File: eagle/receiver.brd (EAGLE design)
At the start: 82.5 x 47.6 mm, 231 parts, among them U1 LTC5566, U4 LTC5566

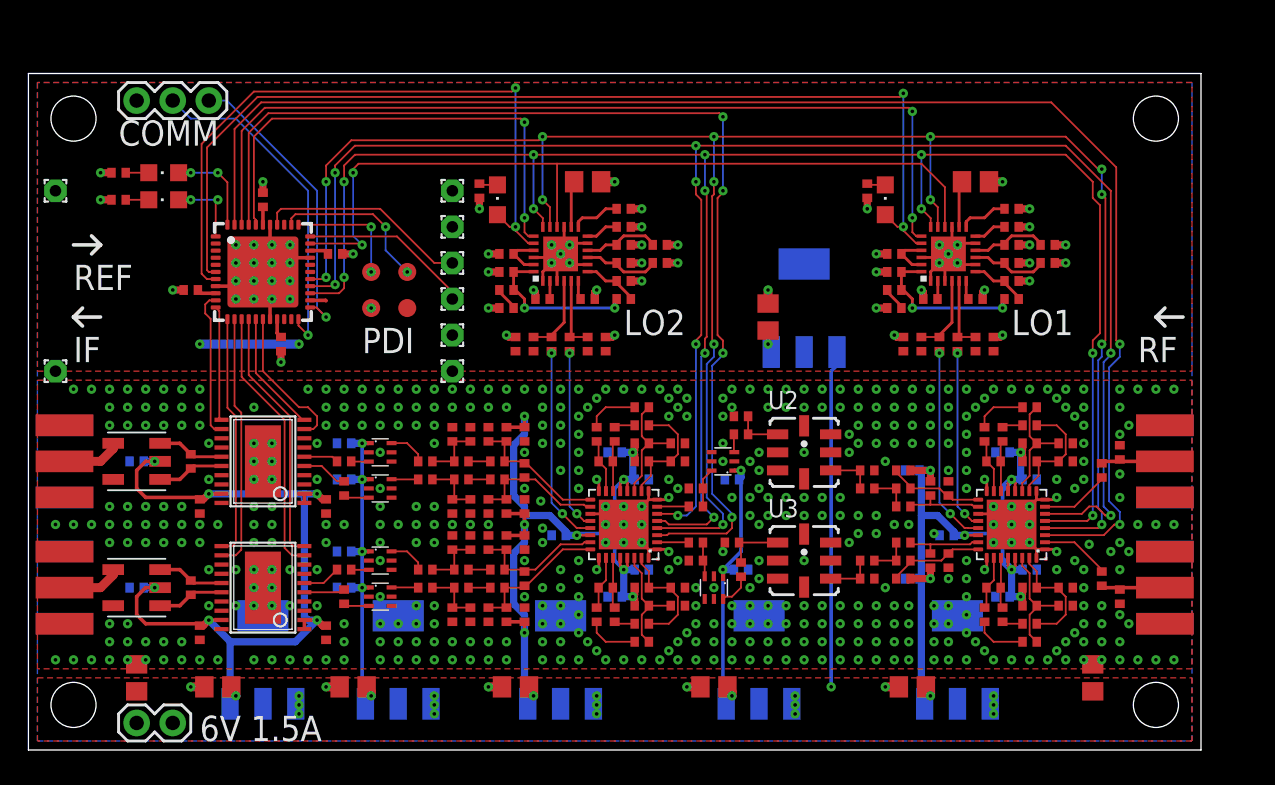
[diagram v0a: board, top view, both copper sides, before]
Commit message: fix issue with receiver board
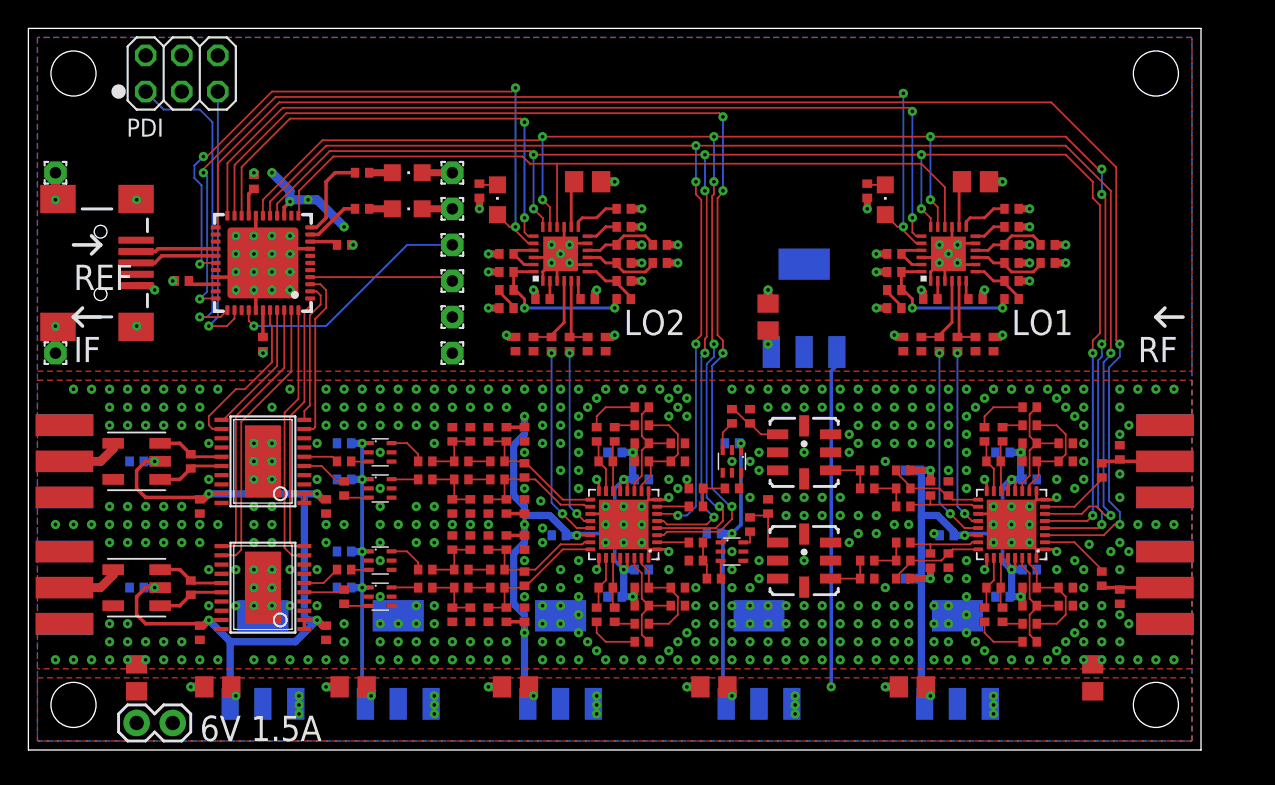
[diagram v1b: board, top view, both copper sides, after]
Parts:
- removed E$21: (no value), atmel:MLF44-TH
- removed E$38: (no value), SparkFun-Connectors:1X03
- removed E$39, E$40, E$41, E$42: (no value), testpad:B1,27
- removed E$45, E$46: (no value), led:CHIPLED_0805
- removed L8: (no value), rcl:R0402
- added D1, D2: (no value), led:CHIPLED_0805
- added J1: (no value), SparkFun-Connectors:USB-MINIB
- added PDI: (no value), pinhead:2X03
- added R1, R2: 330, rcl:R0402
- added R6: 100, rcl:R0402
- added U9: (no value), atmel:MLF44-TH
- C103, C104, C117, C118, C123, C124, C125, C126, C129, C130, C131, C163, C164, C71, C72, C73, C74, C75, C76, C89, C90: value (none) -> 100n
- C132: value (none) -> 1--n
- C45, C77, C78, C81, C82, C83, C84, C87, C88: value (none) -> 10n
- C46: value (none) -> 18p
- C79, C80, C85, C86: value (none) -> 22n
- L3: value (none) -> 11n
- R5: value (none) -> 100
- moved C45 47.7 mm to (49.5, 18.4), turned to 180 degrees
- moved C44 46.5 mm to (49.5, 23.5), turned to 270 degrees
- moved C127 16.3 mm to (50.8, 15.9)
- moved L5 3.59 mm to (52.1, 17.1), turned to 90 degrees
- moved L10 3.18 mm to (48.3, 15.2), turned to 180 degrees
- moved E$5 2.84 mm to (49.5, 14.0), turned to 270 degrees
- moved L9 2.54 mm to (49.5, 21.6)
- moved L6 2.01 mm to (48.3, 12.1), turned to 180 degrees
- moved C71 1.42 mm to (15.9, 40.0)
- moved E$29 1.27 mm to (1.91, 40.6)
- moved E$30 1.27 mm to (29.8, 40.6)
- moved E$33 1.27 mm to (29.8, 35.6)
- moved E$34 1.27 mm to (29.8, 33.0)
- moved E$35 1.27 mm to (29.8, 38.1)
- moved C76 1.27 mm to (16.5, 28.6)
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- renumbered C128 to R5, C161 to R3, C162 to R4, E$1 to J5, E$15 to U5, E$16 to U6, E$17 to J2, E$18 to J3, E$2 to J6, E$3 to U7, E$4 to U8, E$51 to J4, E$52 to T1, E$53 to T2
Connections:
- removed net S$49: E$6.3, L8.2
- removed net S$87: E$13.11, E$21.11
- removed net S$88: E$13.12, E$21.10
- new net LOCK0: E$47.A, U8.20, U9.28
- new net LOCK1: E$48.A, U7.20, U9.33
- new net S$1: J1.D-, U9.26
- new net S$115: E$13.11, U9.41
- new net S$2: J1.D+, U9.27
- net !RESET: now also PDI.5, U9.35; no longer E$21.35, E$40.TP
- net CLK: now also U9.37; no longer E$21.37
- net CLK_100K: now also U9.12; no longer E$21.32
- net CS0: now also U9.20; no longer E$21.40
- net CS1: now also U9.21; no longer E$21.41
- net CS2: now also U9.22; no longer E$21.42
- net CS3: now also U9.23; no longer E$21.43
- net GND: now also D1.C, D2.C, J1.GND, J1.S1, J1.S2, J1.S3, J1.S4, PDI.6, U9.18, U9.30, U9.38, U9.8, U9.TH; no longer C44.1, C45.1, E$21.18, E$21.30, E$21.38, E$21.8, E$21.TH, E$38.1, E$42.TP
- net PDI: now also PDI.1, U9.34; no longer E$21.34, E$41.TP
- net PPS: now also U9.4; no longer E$21.33
- net S$106: now also D1.A, R1.1; no longer C45.2, E$46.C
- net S$109: now also D2.A, R2.1; no longer E$21.44, E$45.A
- net S$110: now also E$13.12, U9.40; no longer E$21.1, E$46.A
- net S$27: now also R1.2, U9.11; no longer E$21.7, E$47.A, U8.20
- net S$28: now also R2.2, U9.10; no longer E$21.23, E$38.3
- net S$29: now also L6.2; no longer E$5.3
- net S$30: now also C45.2; no longer E$6.6
- net S$47: now also R6.1; no longer C127.1
- net S$48: now also R6.2; no longer C127.2
- net S$50: now also C127.1; no longer L6.2
- net S$52: now also C44.1; no longer L8.1
- net S$53: now also C127.2; no longer L6.1
- net S$56: now also C44.2, E$6.3; no longer E$21.22, E$38.2
- net S$69: now also U9.2; no longer E$21.16
- net S$82: now also U9.3; no longer E$21.17
- net S$83: now also U9.1; no longer E$21.15
- net S$84: now also U9.44; no longer E$21.14
- net S$85: now also U9.43; no longer E$21.13
- net S$86: now also U9.42; no longer E$21.12
- net S$96: now also E$5.3, L6.1; no longer E$21.6, E$48.A, U7.20
- net S$97: now also C45.1, E$6.6; no longer C44.2, E$45.C
- net SPI_CLK: now also U9.17; no longer E$21.27
- net SPI_SDI: now also U9.15; no longer E$21.25
- net SPI_SDO: now also U9.16; no longer E$21.26
- net V3.3: now also PDI.2, U9.14, U9.19, U9.31, U9.39, U9.9; no longer E$21.19, E$21.24, E$21.31, E$21.39, E$21.9, E$39.TP
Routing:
- net LOCK1: track 0.00 -> 75.0 mm, vias 0 -> 4
- net S$96: track 73.0 -> 1.27 mm, vias 2 -> 0
- net LOCK0: track 0.00 -> 46.5 mm, vias 0 -> 4
- net S$27: track 47.5 -> 6.24 mm, vias 2 -> 0
- net S$56: track 23.7 -> 2.14 mm, vias 1 -> 0
- net S$28: track 20.8 -> 3.91 mm, vias 1 -> 0
- net PDI: track 8.36 -> 22.1 mm, vias 2 -> 1
- net S$88: track 10.4 -> 0.00 mm
- net S$115: track 0.00 -> 9.42 mm
- net S$87: track 8.08 -> 0.00 mm
- net !RESET: track 11.4 -> 19.4 mm, vias 2 -> 1
- net S$110: track 5.40 -> 11.4 mm, vias 2 -> 0
- net GND: track 76.7 -> 82.6 mm, vias 549 -> 544
- net S$2: track 0.00 -> 5.81 mm
- net S$1: track 0.00 -> 5.69 mm
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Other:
- board size 82.5 x 47.6 mm -> 82.5 x 50.8 mm
- board text removed: "COMM"
- board text removed: "PDI"

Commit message: add power injection to receiver board
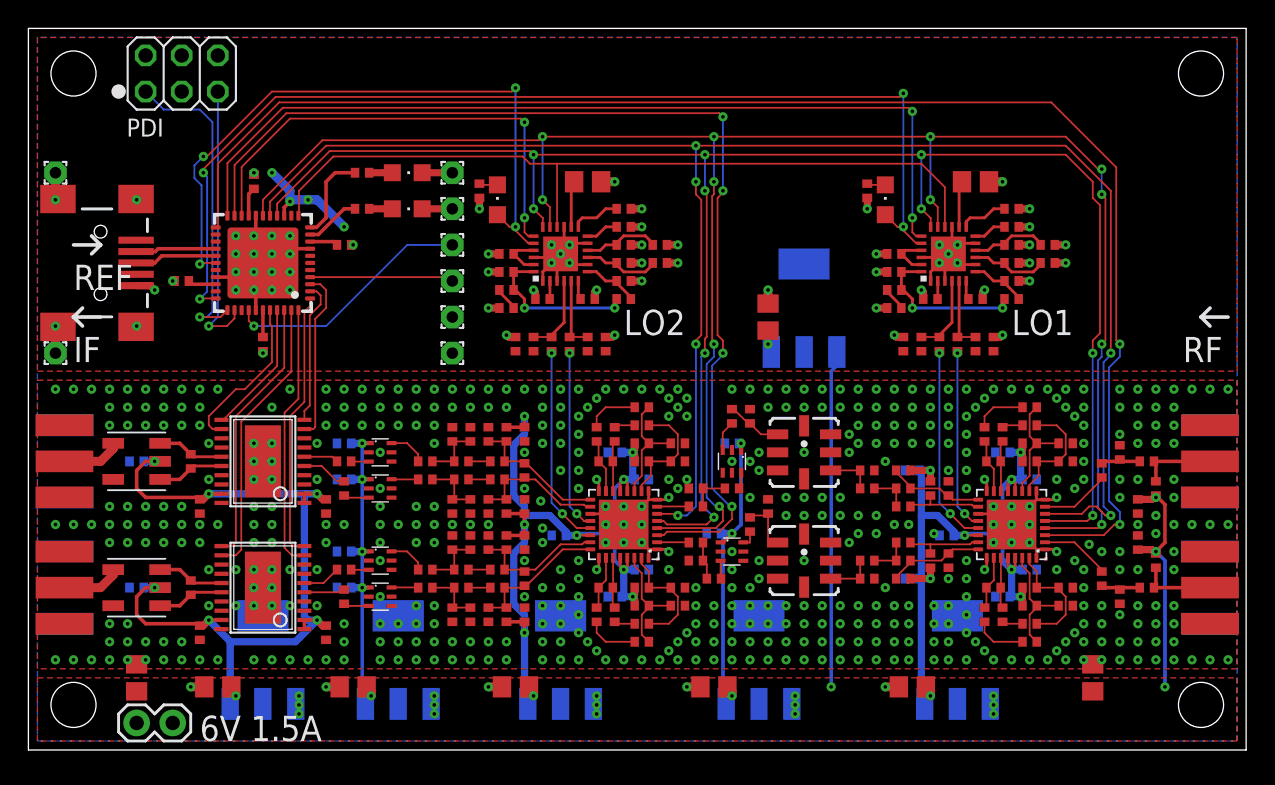
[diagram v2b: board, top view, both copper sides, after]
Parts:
- added C128, C161, C162, C165: 10n, rcl:R0402
- added L11, L8: 22n, rcl:R0402
- C1, C2: value (none) -> 2.8p
- C47: value (none) -> 18p
- E$23, E$24, E$25, E$27, E$49, E$50, E$8: value (none) -> 1u
- L1, L2: value (none) -> 5.8n
- L4: value (none) -> 11n
- L6: value (none) -> 10n
- moved J5 3.17 mm to (83.2, 8.89)
- moved J6 3.17 mm to (83.2, 17.8)
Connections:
- new net S$116: C1.1, C161.1, L1.1
- new net S$117: C128.1, C2.2, L2.1
- net GND: now also C162.1, C165.2
- net RF1: now also C161.2, L8.1; no longer C1.1, L1.1
- net RF2: now also C128.2, L11.2; no longer C2.2, L2.1
- net VIN: now also C162.2, C165.1, L11.1, L8.2
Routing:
- net VIN: track 25.0 -> 42.3 mm, vias 16 -> 19
- net S$117: track 0.00 -> 2.87 mm
- net S$116: track 0.00 -> 2.87 mm
- net RF2: track 4.64 -> 5.35 mm
- net RF1: track 4.64 -> 5.35 mm
- net GND: vias 544 -> 576
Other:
- board size 82.5 x 50.8 mm -> 85.7 x 50.8 mm

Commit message: tweak rf matching network
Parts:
- C1, C2: value 2.8p -> 3p
- L1, L2: value 5.8n -> 7.5n
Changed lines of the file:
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@@
 <element name="J5" library="SparkFun-Retired" library_urn="urn:adsk.eagle:library:533" package="SMA-EDGE" value="" x="83.185" y="8.89" smashed="yes" rot="R90"/>
 <element name="J6" library="SparkFun-Retired" library_urn="urn:adsk.eagle:library:533" package="SMA-EDGE" value="" x="83.185" y="17.78" smashed="yes" rot="R90"/>
-<element name="L1" library="rcl" library_urn="urn:adsk.eagle:library:334" package="R0402" package3d_urn="urn:adsk.eagle:package:23547/3" value="5.8n" x="76.835" y="20.955" smashed="yes" rot="R90"/>
-<element name="C1" library="rcl" library_urn="urn:adsk.eagle:library:334" package="R0402" package3d_urn="urn:adsk.eagle:package:23547/3" value="2.8p" x="75.565" y="19.685" smashed="yes" rot="R270"/>
-<element name="L2" library="rcl" library_urn="urn:adsk.eagle:library:334" package="R0402" package3d_urn="urn:adsk.eagle:package:23547/3" value="5.8n" x="76.835" y="10.795" smashed="yes" rot="R270"/>
-<element name="C2" library="rcl" library_urn="urn:adsk.eagle:library:334" package="R0402" package3d_urn="urn:adsk.eagle:package:23547/3" value="2.8p" x="75.565" y="12.065" smashed="yes" rot="R270"/>
+<element name="L1" library="rcl" library_urn="urn:adsk.eagle:library:334" package="R0402" package3d_urn="urn:adsk.eagle:package:23547/3" value="7.5n" x="76.835" y="20.955" smashed="yes" rot="R90"/>
+<element name="C1" library="rcl" library_urn="urn:adsk.eagle:library:334" package="R0402" package3d_urn="urn:adsk.eagle:package:23547/3" value="3p" x="75.565" y="19.685" smashed="yes" rot="R270"/>
+<element name="L2" library="rcl" library_urn="urn:adsk.eagle:library:334" package="R0402" package3d_urn="urn:adsk.eagle:package:23547/3" value="7.5n" x="76.835" y="10.795" smashed="yes" rot="R270"/>
+<element name="C2" library="rcl" library_urn="urn:adsk.eagle:library:334" package="R0402" package3d_urn="urn:adsk.eagle:package:23547/3" value="3p" x="75.565" y="12.065" smashed="yes" rot="R270"/>
 <element name="U1" library="ref-packages" library_urn="urn:adsk.eagle:library:338" package="HVQFN32" value="LTC5566" x="69.215" y="15.875" smashed="yes" rot="R180"/>
 <element name="C3" library="rcl" library_urn="urn:adsk.eagle:library:334" package="R0402" package3d_urn="urn:adsk.eagle:package:23547/3" value="" x="70.485" y="11.43" smashed="yes">

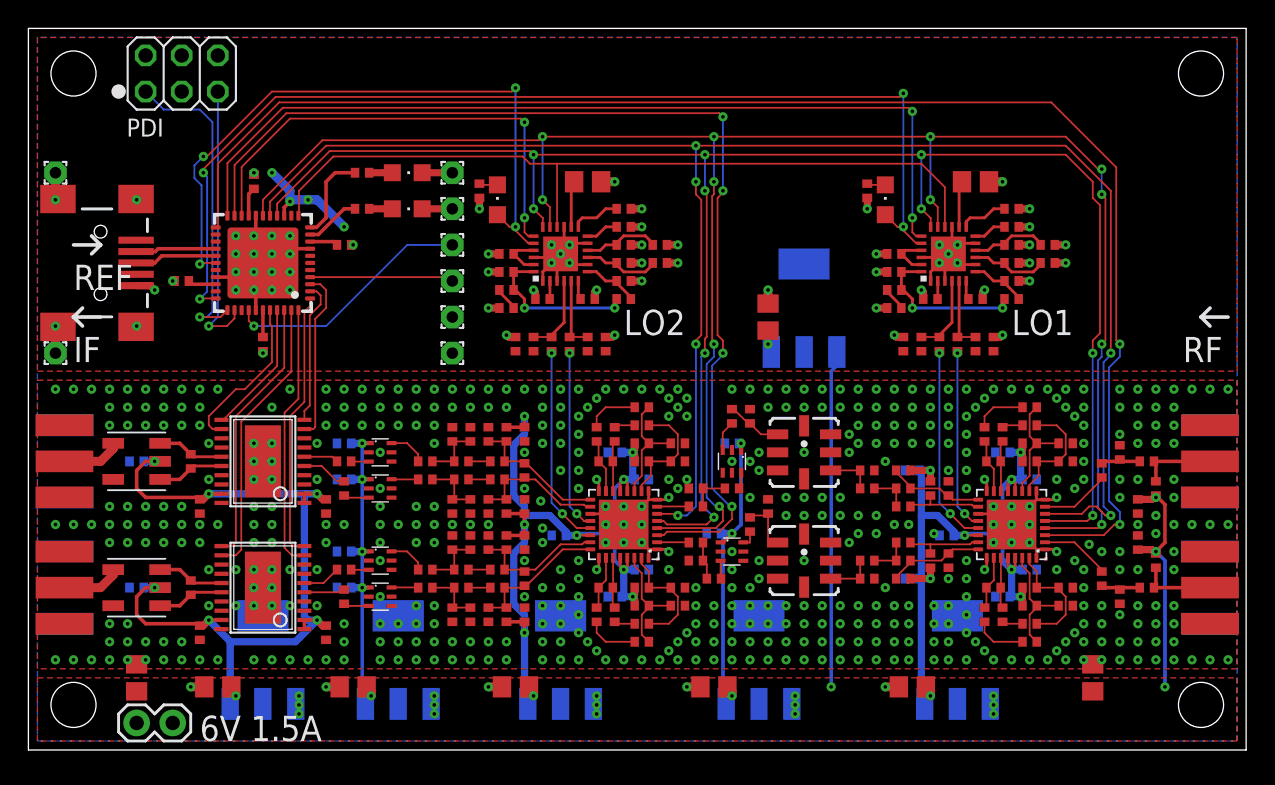
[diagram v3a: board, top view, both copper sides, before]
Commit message: fix saw filter matching
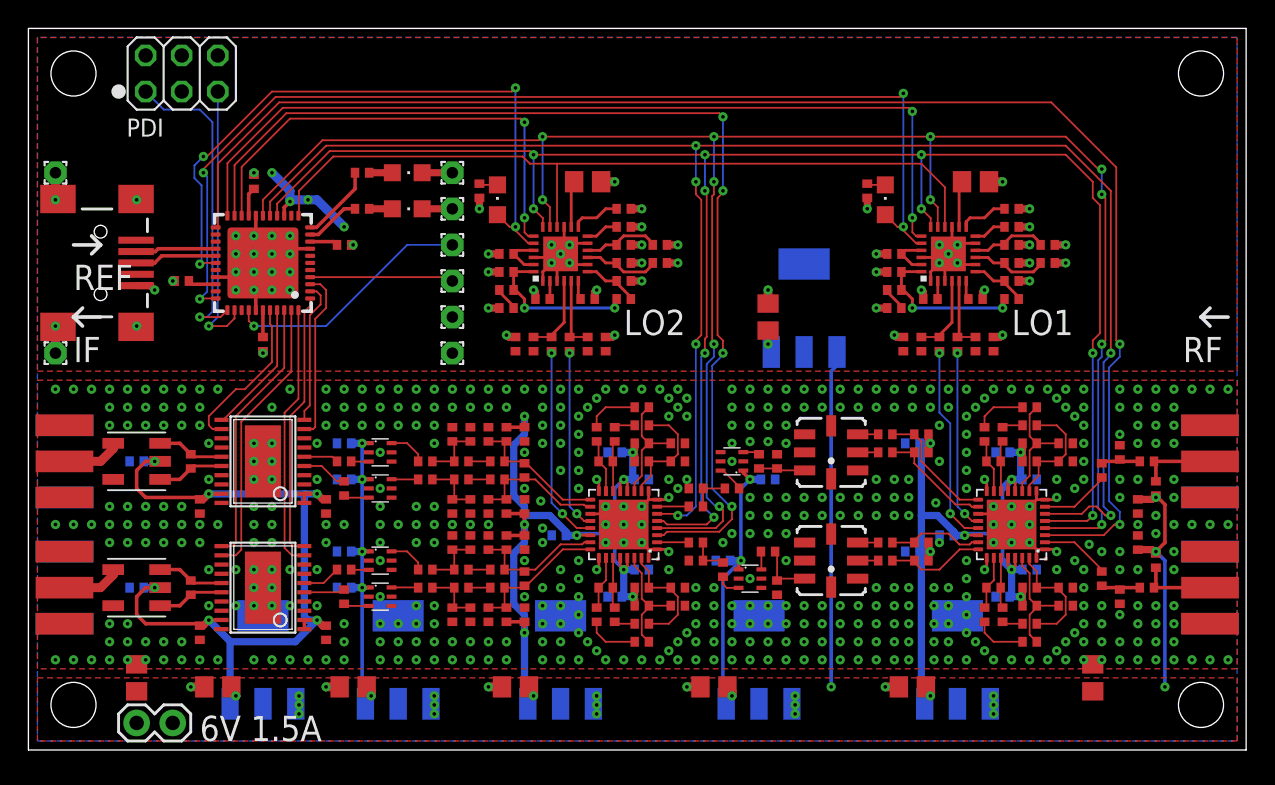
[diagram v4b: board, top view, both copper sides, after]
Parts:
- removed C28, C29, C31, C32, C34, C35, C36, C37, C39, C41: (no value), rcl:R0402
- added L12, L13, L14, L15: 13n, rcl:R0402
- C127, C44: value (none) -> 7p
- C30, C33, C38, C40: value (none) -> 470p
- C42, C43: value (none) -> 10n
- E$44: value (none) -> 1u
- L5, L7: value (none) -> 12n
- U2, U3: value (none) -> AFS374E
- moved L5 5.75 mm to (52.7, 11.4), turned to 270 degrees
- moved C33 4.02 mm to (60.3, 22.2)
- moved C44 3.70 mm to (51.4, 20.3), turned to 90 degrees
- moved L7 3.70 mm to (52.7, 20.3)
- moved L9 3.59 mm to (52.1, 19.1), turned to 0 degrees
- moved C30 2.84 mm to (60.3, 21.0)
- moved C127 2.29 mm to (52.1, 14.0), turned to 0 degrees
- moved E$5 2.29 mm to (50.8, 12.1)
- moved L10 2.01 mm to (48.9, 13.3)
- moved C42 1.91 mm to (62.2, 14.0)
- moved C43 1.91 mm to (62.2, 21.6)
- moved U2 1.91 mm to (56.5, 21.0), turned to 180 degrees
- moved U3 1.91 mm to (56.5, 13.3), turned to 180 degrees
- moved C38 1.80 mm to (60.3, 14.6)
- moved C40 1.27 mm to (60.3, 13.3)
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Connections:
- removed net S$20: C29.1, C31.1, U1.18
- removed net S$23: C35.1, C38.2, C39.2, U1.24
- removed net S$24: C36.1, C37.2, U1.23
- new net S$121: C40.1, U3.2
- new net S$122: C30.2, U2.2
- new net S$123: C33.2, U2.3
- net GND: now also U2.1, U2.5, U3.1, U3.5; no longer C28.2, C34.1, C35.2, C41.2, U2.2, U2.3, U2.7, U3.2, U3.3, U3.7
- net S$17: now also C30.1, L14.1, U1.18; no longer C33.2, C34.2, U2.5
- net S$18: now also C38.1, U3.3; no longer C30.2, C31.2, C33.1
- net S$21: now also C40.2, L13.1, U1.24; no longer C40.1, C41.1, U3.5
- net S$22: now also C38.2, L12.1, U1.23; no longer C37.1, C38.1, C40.2
- net S$25: now also C33.1, L15.1; no longer C28.1, C30.1, C32.1
- net S$52: now also U2.7; no longer U2.1
- net S$53: now also U3.7; no longer U3.1
- net V3.3_2: now also L12.2, L13.2, L14.2, L15.2; no longer C29.2, C32.2, C36.2, C39.1
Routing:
- net S$23: track 6.78 -> 0.00 mm
- net S$20: track 5.54 -> 0.00 mm
- net S$24: track 5.53 -> 0.00 mm
- net S$17: track 3.35 -> 8.51 mm
- net S$22: track 2.81 -> 6.90 mm
- net S$21: track 3.35 -> 6.97 mm
- net S$25: track 6.78 -> 8.77 mm
- net V2.5_2: track 22.7 -> 21.2 mm
- net S$123: track 0.00 -> 1.44 mm
- net S$122: track 0.00 -> 1.44 mm
- net S$121: track 0.00 -> 1.44 mm
- net S$18: track 2.81 -> 1.44 mm
- net S$56: track 2.14 -> 1.17 mm
- net S$27: track 6.24 -> 5.42 mm
- net S$97: track 1.17 -> 1.90 mm
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
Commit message: reorganize eagle files
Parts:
- removed E$22: (no value), transistor-fet:SOT223
- removed E$28, E$29, E$30, E$31, E$32, E$33, E$34, E$35: (no value), wirepad:1,6/0,8
- removed J4: (no value), SparkFun-Connectors:1X02
- added E$1, E$2, E$3, E$4: 1u, rcl:R0805
- added REF: (no value), pinhead:1X03
- moved E$25 3.24 mm to (16.5, 5.08), turned to 90 degrees
- moved D1 0.63 mm to (26.7, 40.0)
- moved J1 0.63 mm to (5.08, 34.9)
- moved R1 0.63 mm to (23.5, 40.0)
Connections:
- new net VBUS: E$3.1, J1.VBUS
- net CLK: now also REF.2; no longer E$33.1
- net GND: now also E$1.2, E$4.1, REF.1; no longer E$22.2, E$22.4, E$28.1, E$29.1, E$30.1, E$31.1, E$35.1, J4.1
- net PPS: now also REF.3; no longer E$34.1
- net V3.3: no longer E$32.1
- net V5: now also C162.2, C165.1, E$1.1, E$19.1, E$2.1, E$20.1, E$26.1, E$43.1, E$49.1, E$50.1, E$7.1, L11.1, L8.2; no longer E$22.3
- net VIN: now also E$2.2, E$3.2, E$4.2; no longer C162.2, C165.1, E$19.1, E$20.1, E$22.1, E$26.1, E$43.1, E$49.1, E$50.1, E$7.1, J4.2, L11.1, L8.2
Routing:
- net V5: track 57.9 -> 110.8 mm, vias 7 -> 24
- net VIN: track 42.3 -> 20.9 mm, vias 19 -> 1
- net VBUS: track 0.00 -> 7.28 mm, vias 0 -> 1
- net CLK: track 17.6 -> 10.7 mm
- net PPS: track 10.1 -> 5.08 mm
- net V3.3: track 28.6 -> 25.3 mm, vias 5 -> 4
- net GND: track 82.6 -> 81.3 mm, vias 580 -> 581
- net S$27: track 5.42 -> 4.78 mm
- added copper zone on layer 1, net V5
- removed copper zone on layer 1, net VIN
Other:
- board text removed: "6V 1.5A"
- board text removed: "REF"
